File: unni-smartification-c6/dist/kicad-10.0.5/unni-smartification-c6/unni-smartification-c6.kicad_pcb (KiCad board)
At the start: 4 copper layers, 83.3 x 65 mm, 74 parts, among them J1 USB-C (replacement daughterbo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, J10 Conn_01x06, J2 Li-Ion 1S JST-PH, J3 Conn_01x06, J4 UNNI DC / battery input - AC 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, J5 Conn_01x02, J6 Conn_01x05, Q1 AO3401A, Q10 AO3400A touch emulator, Q2 AO3401A, Q3 AO3400A, Q4 AO3400A, SW1 RESET, SW2 BOOT, U1 MCP73831T-2ACI/OT, U10 ESP32-C6-MINI-1, U2 TPS63031DSK, U3 TPS613222ADBZ (5V), U4 TPD2E009DBZR

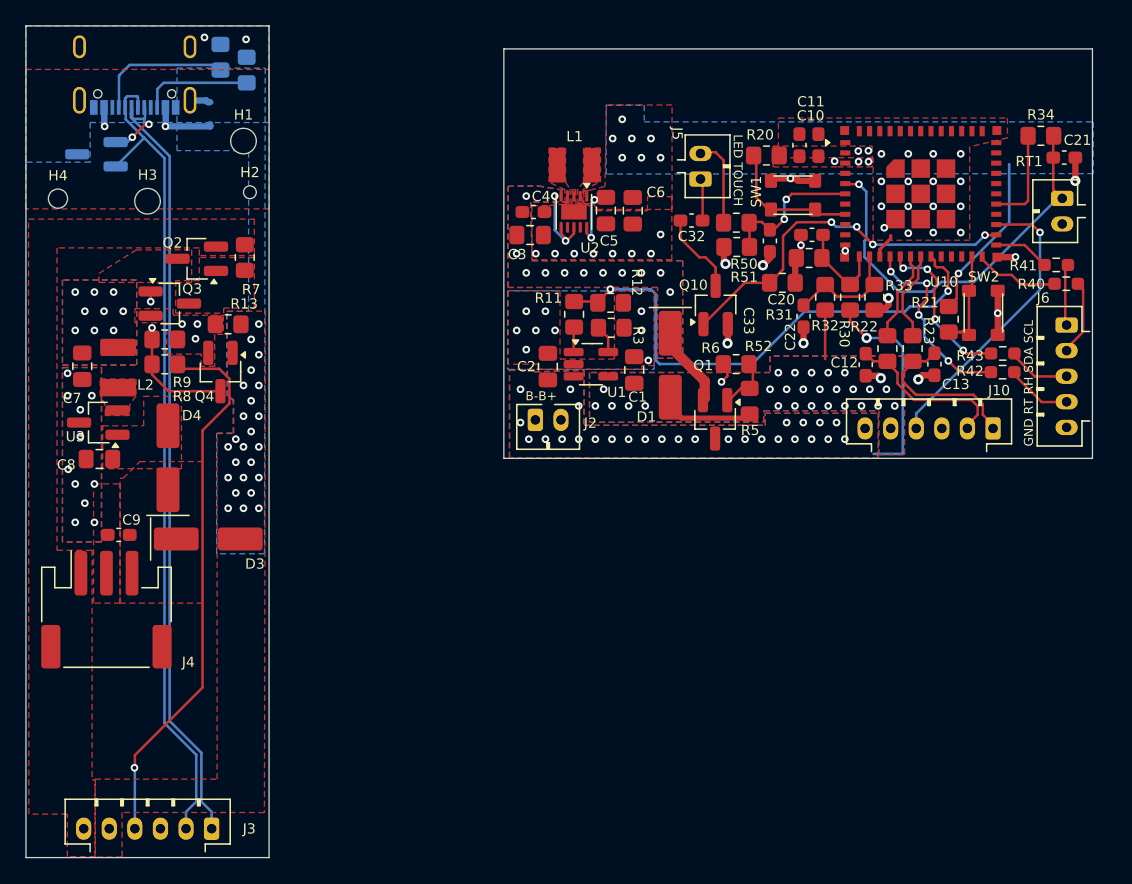
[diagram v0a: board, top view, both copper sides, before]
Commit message: redid some routing, add btn for manual measurements from unni
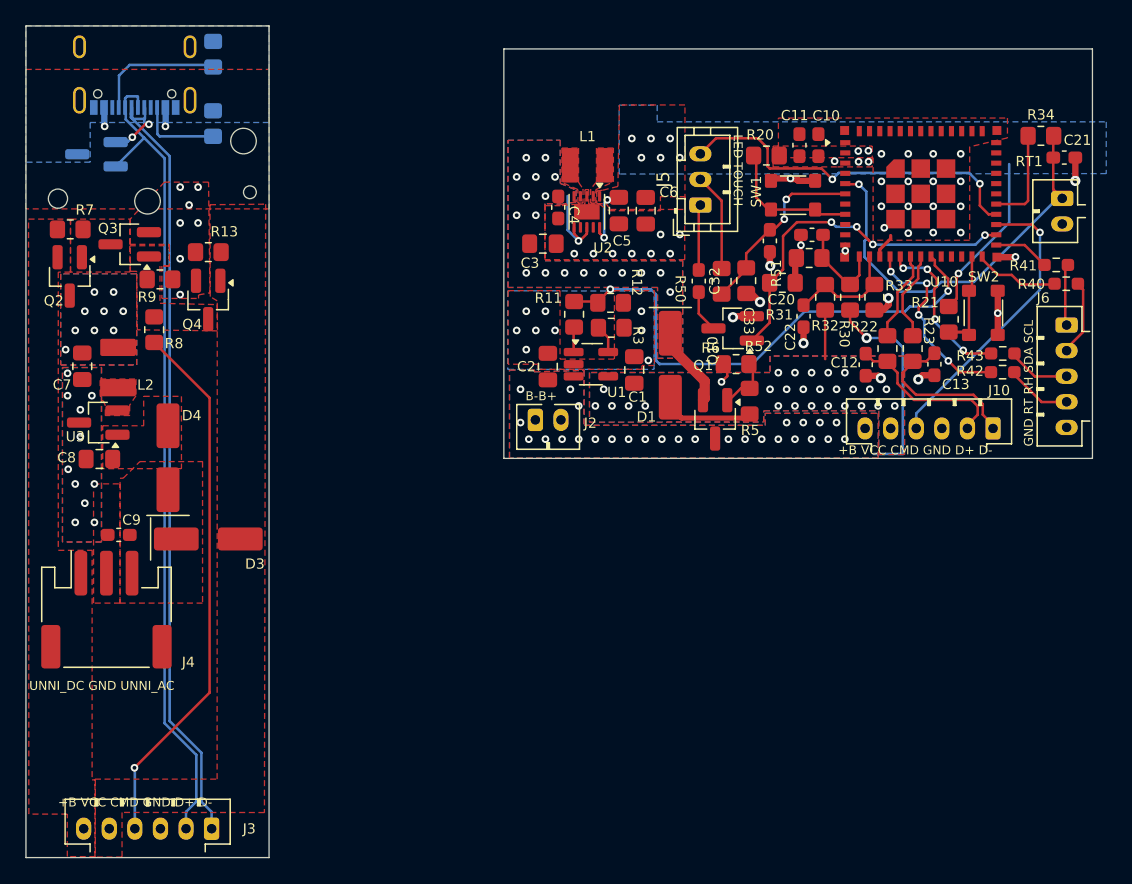
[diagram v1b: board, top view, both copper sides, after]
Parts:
- J5: footprint Connector_JST:JST_PH_B2B-PH-K_1x02_P2.00mm_Vertical -> Connector_JST:JST_PH_B3B-PH-K_1x03_P2.00mm_Vertical
- moved R7 13.8 mm to (76.1, 139.1), turned to 180 degrees
- moved Q2 10.0 mm to (76.1, 142.8), turned to -90 degrees
- moved R13 5.85 mm to (86.9, 140.9)
- moved Q4 5.71 mm to (86.9, 144.6)
- moved Q3 5.59 mm to (80.8, 140.3), turned to 180 degrees
- moved R2 4.94 mm to (87.3, 130.8)
- moved C32 4.76 mm to (125.2, 143.1), turned to -90 degrees
- moved R50 4.72 mm to (127.0, 143.2), turned to -90 degrees
- moved R9 4.71 mm to (83.1, 143.0)
- moved R8 2.83 mm to (82.7, 146.9), turned to 90 degrees
- moved R51 2.73 mm to (128.9, 143.1), turned to -90 degrees
- moved Q10 2.26 mm to (127.9, 146.8), turned to 180 degrees
- moved J5 2.03 mm to (125.4, 137.2)
- moved C4 1.97 mm to (114.2, 137.4), turned to -90 degrees
- moved C3 1.21 mm to (113.0, 140.2)
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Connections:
- U10 pad 28: unconnected-(U10-IO22-Pad28) -> CONN_BTN
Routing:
- net CONN_BTN: track 0.00 -> 28.3 mm, vias 0 -> 2
- net Net-(Q3-G): track 12.4 -> 0.00 mm, vias 2 -> 0
- net VBUS: track 18.0 -> 14.3 mm, vias 52 -> 28
- net Net-(Q10-D): track 6.56 -> 3.31 mm
- net BACKLIGHT_ADC: track 11.7 -> 14.5 mm
- net Net-(J1-CC2): track 8.64 -> 6.48 mm
- net CONN_TOUCH: track 3.31 -> 5.13 mm
- net GND: track 30.4 -> 28.6 mm, vias 63 -> 65
- net TOUCH_TRIGGER: track 28.8 -> 27.4 mm
- net Net-(J1-CC1): track 11.0 -> 10.3 mm
- net CONN_LED+: track 6.98 -> 7.65 mm
- net SYS: vias 13 -> 19
- net +3V3: vias 15 -> 14
- added copper zone on F.Cu, net Net-(Q3-G)
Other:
- board text added: "+B VCC CMD GND D+ D-"
- board text added: "UNNI_DC GND UNNI_AC"

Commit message: some silkscreen changes
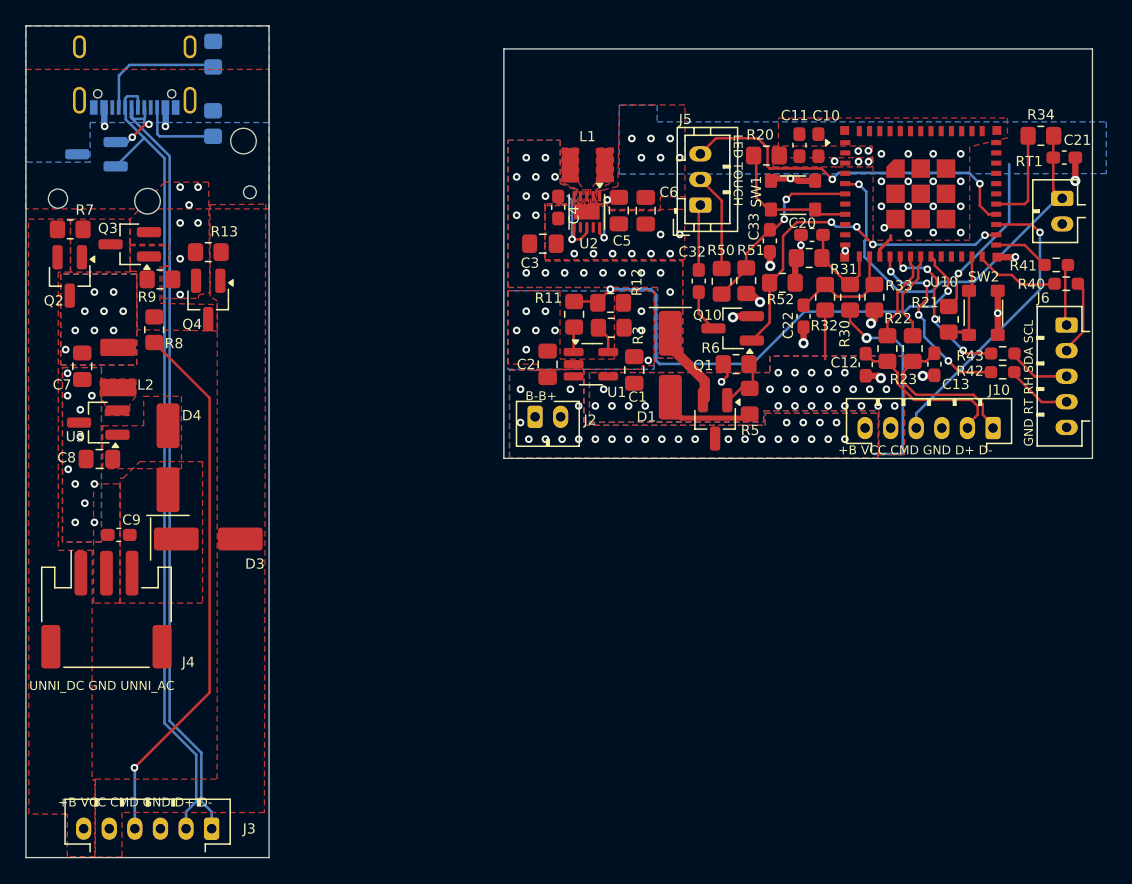
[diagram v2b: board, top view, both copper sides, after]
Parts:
- moved J2 0.24 mm to (112.4, 153.8)
- moved C2 0.18 mm to (113.4, 149.7)
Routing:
- net GND: track 28.6 -> 27.5 mm

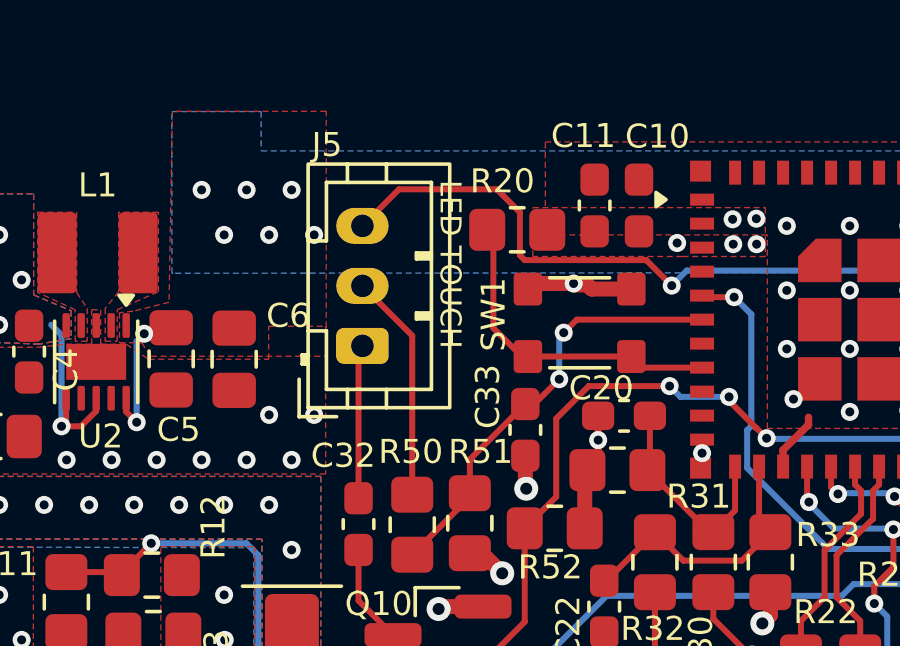
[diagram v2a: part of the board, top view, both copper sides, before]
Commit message: Prepare Rev A prototype and add PCBWay sponsorship
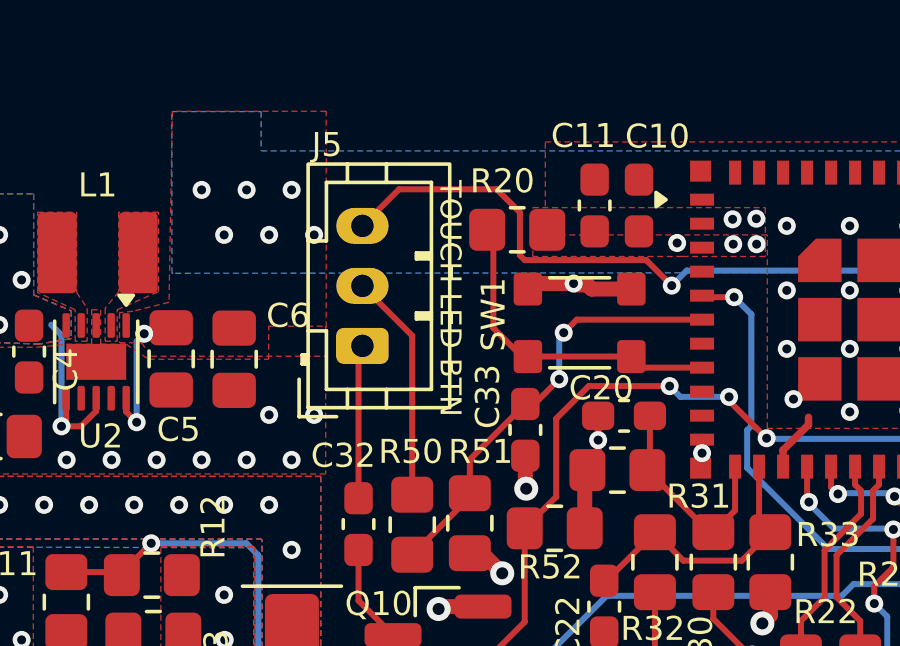
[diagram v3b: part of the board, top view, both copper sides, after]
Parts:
- C32: value 220pF DNP -> 220pF
- J5: value Conn_01x02 -> Conn_01x03
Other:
- board text added: "TOUCH LED BTN"
- board text removed: "LED TOUCH"
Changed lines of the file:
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@@
 			)
 		)
-		(property "Value" "Conn_01x02"
+		(property "Value" "Conn_01x03"
 			(at 2 4 90)
 			(layer "F.Fab")
@@
 			)
 		)
-		(property "Value" "220pF DNP"
+		(property "Value" "220pF"
 			(at 0 1.43 90)
 			(layer "F.Fab")
@@
 		)
 	)
-	(gr_text "LED TOUCH"
+	(gr_text "TOUCH LED BTN"
 		(at 127.88 131.67 270)
 		(layer "F.SilkS" knockout)

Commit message: Add BOM Metadata, iBom, fix validation, pcbway order
this is the state the PCBs were ordered at PCBWay.com

Thank you PCBWay for sponsoring the boards for this ridicoulus project!
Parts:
- added R24: 10K, Resistor_SMD:R_0603_1608Metric_Pad0.98x0.95mm_HandSolder, B.Cu at (147.2, 137.5)
- D3: value SS14 USB -> UNNI_AC -> SS14
- D4: value SS14 BOOST -> UNNI_AC -> SS14
- J1: value USB-C (replacement daughterboard) -> UJ20-C-H-G-SMT-1-P16-TR
- J10, J3: value Conn_01x06 -> B6B-PH-K-S
- J2: value Li-Ion 1S JST-PH -> B2B-PH-K-S
- J4: value UNNI DC / battery input - AC / 5V Input -> S3B-PH-SM4-TB
- J5: value Conn_01x03 -> B3B-PH-K-S
- J6: value Conn_01x05 -> B5B-PH-K-S
- Q10: value AO3400A touch emulator -> AO3400A
- RT1: value 10k NTC @25C -> NTCC-10K
- U1: value MCP73831T-2ACI/OT -> MCP73831
- U10: value ESP32-C6-MINI-1 -> ESP32-C6-MINI-1-N4
- U2: value TPS63031DSK -> TPS63031
- U3: value TPS613222ADBZ (5V) -> TPS613222A
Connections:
- U10 pad 28: CONN_BTN -> Net-(U10-IO22)
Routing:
- net CONN_BTN: track 28.3 -> 26.1 mm
- net Net-(U10-IO22): track 0.00 -> 2.23 mm, vias 0 -> 1
